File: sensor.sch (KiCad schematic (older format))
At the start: 16 parts, among them U6 VCNT2020, U7 VCNT2020, U8 VCNT2020, U9 VCNT2020

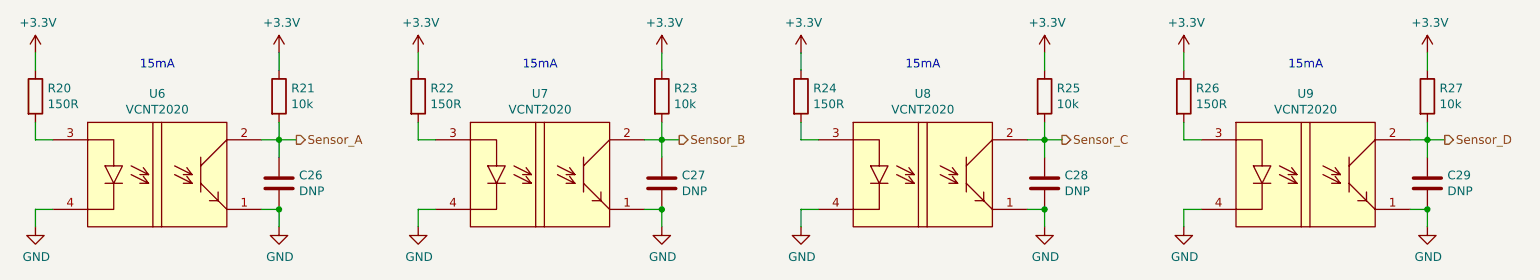
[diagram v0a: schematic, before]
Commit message: Added an optional power output header Changed the resistors for the VCNT2020 to improve performance
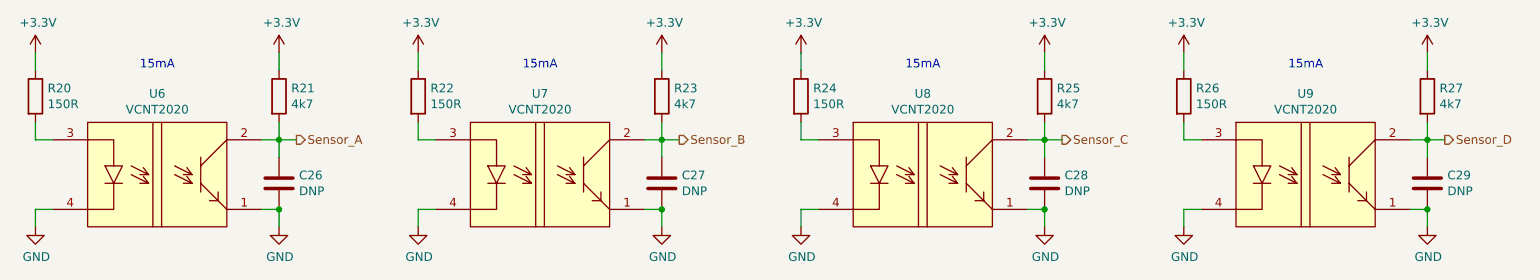
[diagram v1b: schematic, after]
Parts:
- R21, R23, R25, R27: value 10k -> 4k7; lcsc# C128781 -> C304093; manf# TC0325F1002T5E -> AR03FTD4701
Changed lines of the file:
@@
 Sheet 6 6
 Title "MiniFeed"
-Date "2021-01-17"
+Date "2021-02-25"
 Rev "1.0"
 Comp "SG-O"
@@
 AR Path="/6047D150/6049A4B4" Ref="R23"  Part="1"
 F 0 "R23" H 5170 2596 50  0000 L CNN
-F 1 "10k" H 5170 2505 50  0000 L CNN
+F 1 "4k7" H 5170 2505 50  0000 L CNN
 F 2 "Resistor_SMD:R_0603_1608Metric" V 5030 2550 50  0001 C CNN
 F 3 "~" H 5100 2550 50  0001 C CNN
-F 4 "C128781" H 5100 2550 50  0001 C CNN "lcsc#"
-F 5 "TC0325F1002T5E" H 5100 2550 50  0001 C CNN "manf#"
+F 4 "C304093" H 5100 2550 50  0001 C CNN "lcsc#"
+F 5 "AR03FTD4701" H 5100 2550 50  0001 C CNN "manf#"
 	1    5100 2550
 	1    0    0    -1
@@
 AR Path="/6047D150/6049A4C6" Ref="R21"  Part="1"
 F 0 "R21" H 2970 2596 50  0000 L CNN
-F 1 "10k" H 2970 2505 50  0000 L CNN
+F 1 "4k7" H 2970 2505 50  0000 L CNN
 F 2 "Resistor_SMD:R_0603_1608Metric" V 2830 2550 50  0001 C CNN
 F 3 "~" H 2900 2550 50  0001 C CNN
-F 4 "C128781" H 2900 2550 50  0001 C CNN "lcsc#"
-F 5 "TC0325F1002T5E" H 2900 2550 50  0001 C CNN "manf#"
+F 4 "C304093" H 2900 2550 50  0001 C CNN "lcsc#"
+F 5 "AR03FTD4701" H 2900 2550 50  0001 C CNN "manf#"
 	1    2900 2550
 	1    0    0    -1
@@
 AR Path="/6047D150/604EAF63" Ref="R27"  Part="1"
 F 0 "R27" H 9570 2596 50  0000 L CNN
-F 1 "10k" H 9570 2505 50  0000 L CNN
+F 1 "4k7" H 9570 2505 50  0000 L CNN
 F 2 "Resistor_SMD:R_0603_1608Metric" V 9430 2550 50  0001 C CNN
 F 3 "~" H 9500 2550 50  0001 C CNN
-F 4 "C128781" H 9500 2550 50  0001 C CNN "lcsc#"
-F 5 "TC0325F1002T5E" H 9500 2550 50  0001 C CNN "manf#"
+F 4 "C304093" H 9500 2550 50  0001 C CNN "lcsc#"
+F 5 "AR03FTD4701" H 9500 2550 50  0001 C CNN "manf#"
 	1    9500 2550
 	1    0    0    -1
@@
 AR Path="/6047D150/604EAF7C" Ref="R25"  Part="1"
 F 0 "R25" H 7370 2596 50  0000 L CNN
-F 1 "10k" H 7370 2505 50  0000 L CNN
+F 1 "4k7" H 7370 2505 50  0000 L CNN
 F 2 "Resistor_SMD:R_0603_1608Metric" V 7230 2550 50  0001 C CNN
 F 3 "~" H 7300 2550 50  0001 C CNN
-F 4 "C128781" H 7300 2550 50  0001 C CNN "lcsc#"
-F 5 "TC0325F1002T5E" H 7300 2550 50  0001 C CNN "manf#"
+F 4 "C304093" H 7300 2550 50  0001 C CNN "lcsc#"
+F 5 "AR03FTD4701" H 7300 2550 50  0001 C CNN "manf#"
 	1    7300 2550
 	1    0    0    -1
